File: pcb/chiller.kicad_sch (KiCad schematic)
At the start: 53 parts, among them J1 Conn_01x03, J10 Current Sense, J11 Display, J12 Debug, J13 Conn_01x04, J14 Flow sensor, J15 Fan, J2 Conn_01x03, J3 Ext, J4 Conn_01x02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

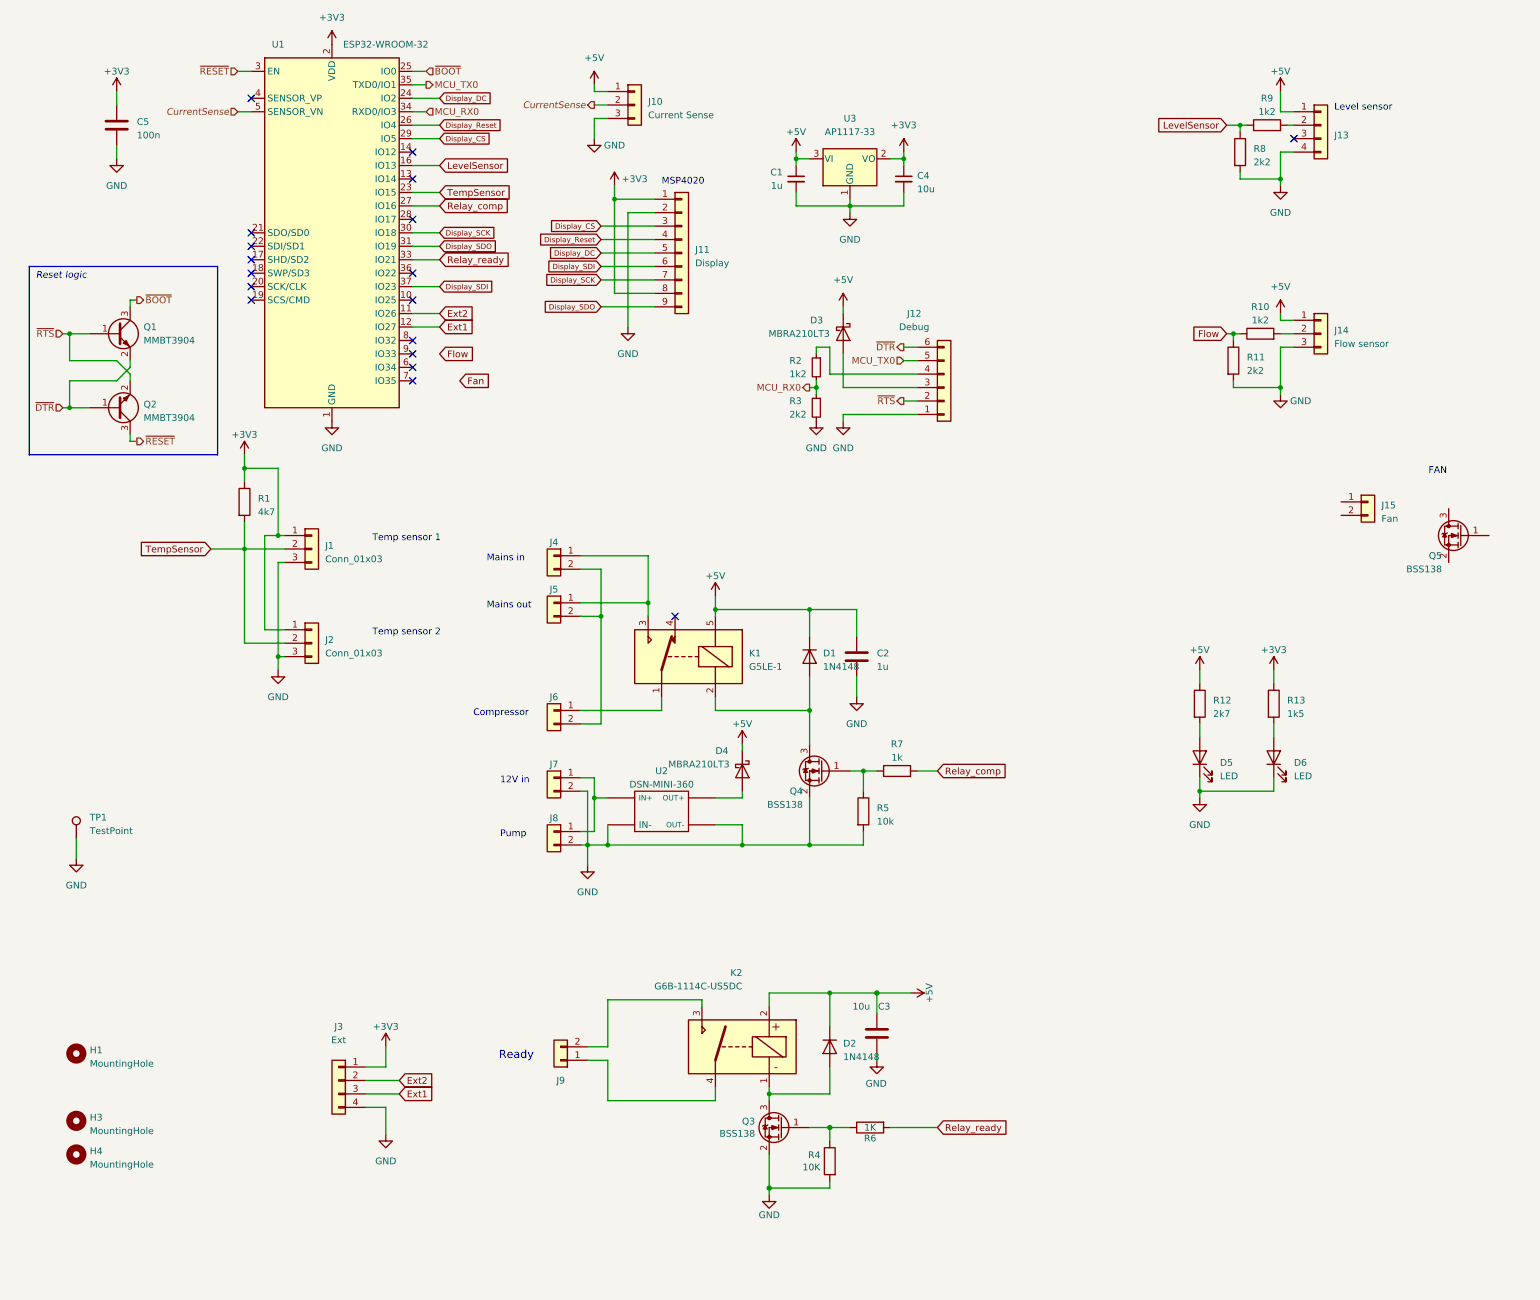
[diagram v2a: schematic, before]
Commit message: Version 2 ready for ordering.
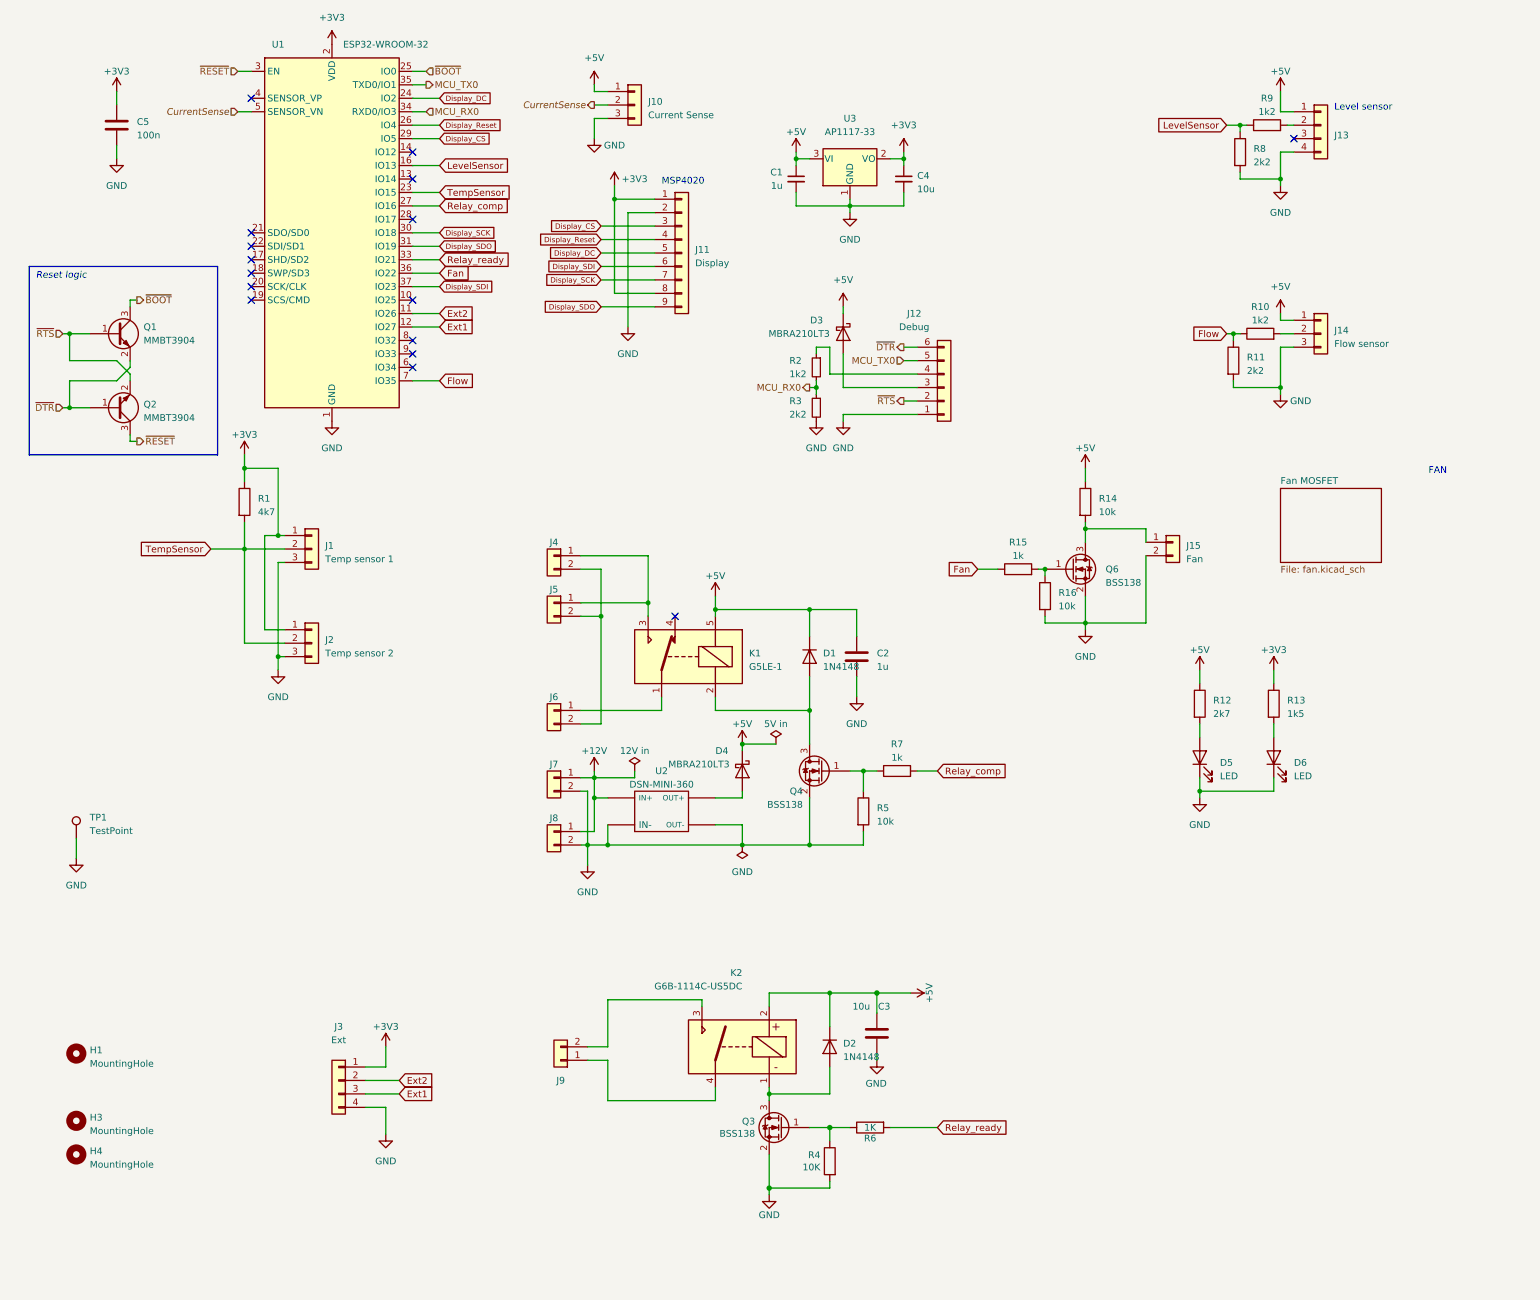
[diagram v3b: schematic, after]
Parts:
- removed Q5: BSS138, Package_TO_SOT_SMD:SOT-23, symbol Device:Q_NMOS_GSD
- added Q6: BSS138, Package_TO_SOT_SMD:SOT-23, symbol Device:Q_NMOS_GSD
- added R14, R16: 10k, Resistor_SMD:R_0603_1608Metric, symbol Device:R
- added R15: 1k, Resistor_SMD:R_0603_1608Metric, symbol Device:R
- J1: value Conn_01x03 -> Temp sensor 1
- J2: value Conn_01x03 -> Temp sensor 2
- J4: value Conn_01x02 -> Mains in
- J5: value Conn_01x02 -> Mains out
- J6: value Conn_01x02 -> Compressor
- J7: value Conn_01x02 -> 12V in
- J8: value Conn_01x02 -> Pump
- J9: value CONN_01X02 -> Ready
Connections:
- net +5V: now also R14.1
- net Fan: now also U1.36 (IO22), R15.1
- net Flow: now also U1.7 (IO35)
- net GND: now also J15.2 (Pin_2), Q6.2 (S), R16.2
- net at J15.1 (Pin_1): now also Q6.3 (D), R14.2
- net +12V: now reaches J7.1 (Pin_1), J8.1 (Pin_1), U2.IN+
- new net: Q6.1 (G), R15.2, R16.1
- no-connect marks 18 -> 16
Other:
- added sheet Fan MOSFET (fan.kicad_sch)
- note removed: "12V in"
- note removed: "Compressor"
- note removed: "Mains in"
- note removed: "Mains out"
- note removed: "Pump"
- note removed: "Ready"
- note removed: "Temp sensor 1"
- note removed: "Temp sensor 2"
- moved on the sheet: J15

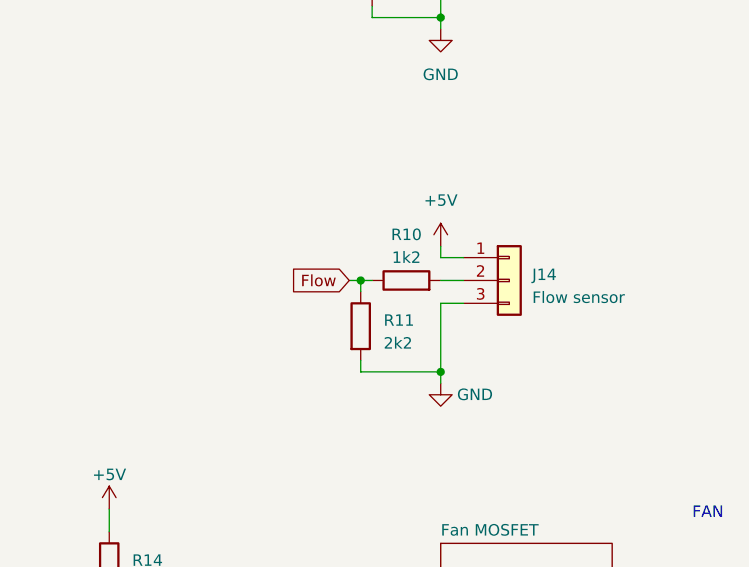
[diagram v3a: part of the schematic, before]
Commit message: Update R10/R11 values
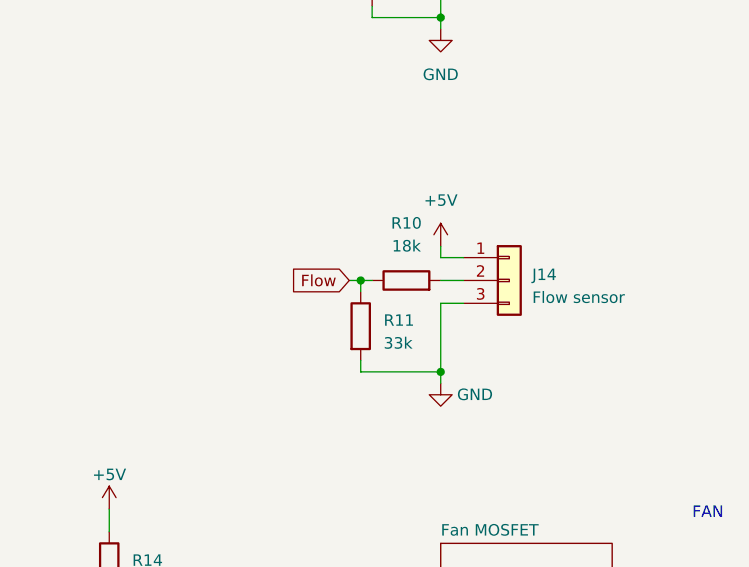
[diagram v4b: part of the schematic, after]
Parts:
- R10: value 1k2 -> 18k
- R11: value 2k2 -> 33k
